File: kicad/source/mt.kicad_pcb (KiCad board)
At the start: 2 copper layers, 65 parts, among them IC1 MCP73831T-2ACI_OT, IC2 BQ29728DSER, IC3 TLV74333PDBVR, IC4 TLV9152IDR, IC5 MSPM0G3507SPMR, IC5 RT9167A-33GB, IC6 IS62WV1288BLL-55QLI, IC7 DAC082S085CIMMX_NOPB, IC8 SN74HC148NSR, IC8 TPS613222ADBVR, J1 694106301002, J2 SJ1-3524N, J3 Conn_01x05_MountingPin, J4 Conn_01x09_MountingPin, Q1 CSD16406Q3, Q2 CSD16406Q3, U1 1043

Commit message: completed full schematic
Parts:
- removed the C1 at (205.4, 44.4)
- removed the C1 at (205.4, 46.4)
- removed the C4 at (205.4, 50.3)
- removed the C4 at (111.7, 113.8)
- removed the C5 at (192.6, 59.5)
- removed the C5 at (121.5, 111.5)
- removed C6: 47u, Capacitor_SMD:C_0805_2012Metric
- removed C7: 4.7u, Capacitor_SMD:C_0402_1005Metric
- removed C7: 100n, Capacitor_SMD:C_1206_3216Metric
- removed C8: 10u, Capacitor_SMD:C_0603_1608Metric
- removed the IC5 at (149.8, 100.2)
- removed the IC5 at (183.8, 84.9)
- removed the IC8 at (183.8, 89.5)
- removed the IC8 at (177.9, 76.6)
- removed L1: 2.2u, Inductor_SMD:L_1008_2520Metric
- removed the R11 at (108.2, 110.3)
- removed the R11 at (108.2, 108.3)
- removed the R12 at (108.2, 106.3)
- removed the R12 at (108.2, 112.3)
- removed the R7 at (163.3, 96.7)
- removed the R7 at (108.2, 102.4)
- removed the R8 at (108.2, 104.4)
- removed the R8 at (163.3, 98.7)
- added C1: 10u, Capacitor_SMD:C_0402_1005Metric, F.Cu at (177.6, 58.8)
- added C21: 10u, Capacitor_SMD:C_0402_1005Metric, F.Cu at (183.3, 64.7)
- added C22: 10u, Capacitor_SMD:C_0402_1005Metric, F.Cu at (186.2, 58.8)
- added C23: 10u, Capacitor_SMD:C_0402_1005Metric, F.Cu at (186.2, 60.7)
- added C24: 10u, Capacitor_SMD:C_0402_1005Metric, F.Cu at (186.2, 62.7)
- added C25: 10u, Capacitor_SMD:C_0402_1005Metric, F.Cu at (186.2, 64.7)
- added C4: 10u, Capacitor_SMD:C_0402_1005Metric, F.Cu at (177.6, 62.7)
- added C5: 22u, Capacitor_SMD:C_0603_1608Metric, F.Cu at (191.3, 96.1)
- added IC10: SN74HC148NSR, SN74HC148NSR:SOIC127P780X200-16N, F.Cu at (122.2, 139.3)
- added IC11: SN74HC148NSR, SN74HC148NSR:SOIC127P780X200-16N, F.Cu at (132.7, 139.3)
- added IC5: MSPM0G3507SPMR, MSPM0G3507SPMR:QFP50P1200X1200X160-64N, F.Cu at (183.4, 50.5)
- added IC8: SN74HC148NSR, SN74HC148NSR:SOIC127P780X200-16N, F.Cu at (101.2, 139.3)
- added IC9: SN74HC148NSR, SN74HC148NSR:SOIC127P780X200-16N, F.Cu at (111.7, 139.3)
- added R11: 100k, Resistor_SMD:R_0402_1005Metric, F.Cu at (182.5, 106.0)
- added R12: 100k, Resistor_SMD:R_0402_1005Metric, F.Cu at (182.5, 108.0)
- added R15: 100k, Resistor_SMD:R_0402_1005Metric, F.Cu at (182.5, 114.0)
- added R16: 100k, Resistor_SMD:R_0402_1005Metric, F.Cu at (182.5, 115.9)
- added R17: 100k, Resistor_SMD:R_0402_1005Metric, F.Cu at (182.5, 117.9)
- added R18: 100k, Resistor_SMD:R_0402_1005Metric, F.Cu at (182.5, 119.9)
- added R19: 100k, Resistor_SMD:R_0402_1005Metric, F.Cu at (182.5, 121.9)
- added R20: 100k, Resistor_SMD:R_0402_1005Metric, F.Cu at (182.5, 123.9)
- added R21: 100k, Resistor_SMD:R_0402_1005Metric, F.Cu at (185.4, 106.0)
- added R22: 100k, Resistor_SMD:R_0402_1005Metric, F.Cu at (185.4, 108.0)
- added R23: 100k, Resistor_SMD:R_0402_1005Metric, F.Cu at (185.4, 110.0)
- added R24: 100k, Resistor_SMD:R_0402_1005Metric, F.Cu at (185.4, 112.0)
- added R25: 100k, Resistor_SMD:R_0402_1005Metric, F.Cu at (185.4, 114.0)
- added R26: 100k, Resistor_SMD:R_0402_1005Metric, F.Cu at (185.4, 115.9)
- added R27: 100k, Resistor_SMD:R_0402_1005Metric, F.Cu at (185.4, 117.9)
- added R28: 100k, Resistor_SMD:R_0402_1005Metric, F.Cu at (185.4, 119.9)
- added R29: 100k, Resistor_SMD:R_0402_1005Metric, F.Cu at (185.4, 121.9)
- added R30: 100k, Resistor_SMD:R_0402_1005Metric, F.Cu at (185.4, 123.9)
- added R31: 100k, Resistor_SMD:R_0402_1005Metric, F.Cu at (188.3, 106.0)
- added R32: 100k, Resistor_SMD:R_0402_1005Metric, F.Cu at (188.3, 108.0)
- added R33: 100k, Resistor_SMD:R_0402_1005Metric, F.Cu at (188.3, 110.0)
- added R34: 100k, Resistor_SMD:R_0402_1005Metric, F.Cu at (188.3, 112.0)
- added R35: 100k, Resistor_SMD:R_0402_1005Metric, F.Cu at (188.3, 114.0)
- added R36: 100k, Resistor_SMD:R_0402_1005Metric, F.Cu at (188.3, 115.9)
- added R37: 100k, Resistor_SMD:R_0402_1005Metric, F.Cu at (188.3, 117.9)
- added R38: 100k, Resistor_SMD:R_0402_1005Metric, F.Cu at (188.3, 119.9)
- added R39: 100k, Resistor_SMD:R_0402_1005Metric, F.Cu at (188.3, 121.9)
- added R40: 100k, Resistor_SMD:R_0402_1005Metric, F.Cu at (188.3, 123.9)
- added R41: 100k, Resistor_SMD:R_0402_1005Metric, F.Cu at (191.2, 106.0)
- added R42: 100k, Resistor_SMD:R_0402_1005Metric, F.Cu at (191.2, 108.0)
- added R43: 100k, Resistor_SMD:R_0402_1005Metric, F.Cu at (191.2, 110.0)
- added R44: 100k, Resistor_SMD:R_0402_1005Metric, F.Cu at (191.2, 112.0)
- added R45: 100k, Resistor_SMD:R_0402_1005Metric, F.Cu at (191.2, 114.0)
- added R46: 100k, Resistor_SMD:R_0402_1005Metric, F.Cu at (191.2, 115.9)
- added R47: 100k, Resistor_SMD:R_0402_1005Metric, F.Cu at (191.2, 117.9)
- added R48: 100k, Resistor_SMD:R_0402_1005Metric, F.Cu at (191.2, 119.9)
- added R49: 100k, Resistor_SMD:R_0402_1005Metric, F.Cu at (191.2, 121.9)
- added R7: 10k, Resistor_SMD:R_0402_1005Metric, F.Cu at (179.6, 117.9)
- added R8: 10k, Resistor_SMD:R_0402_1005Metric, F.Cu at (179.6, 119.9)
- added S10: TL6800AF160QJ, TL6800AF160QJ:TL6800AF160QJ, F.Cu at (114.9, 81.5)
- added S11: TL6800AF160QJ, TL6800AF160QJ:TL6800AF160QJ, F.Cu at (114.9, 91.0)
- added S12: TL6800AF160QJ, TL6800AF160QJ:TL6800AF160QJ, F.Cu at (114.9, 100.3)
- added S13: TL6800AF160QJ, TL6800AF160QJ:TL6800AF160QJ, F.Cu at (114.9, 109.8)
- added S14: TL6800AF160QJ, TL6800AF160QJ:TL6800AF160QJ, F.Cu at (114.9, 119.2)
- added S15: TL6800AF160QJ, TL6800AF160QJ:TL6800AF160QJ, F.Cu at (114.9, 128.6)
- added S16: TL6800AF160QJ, TL6800AF160QJ:TL6800AF160QJ, F.Cu at (127.5, 72.2)
- added S17: TL6800AF160QJ, TL6800AF160QJ:TL6800AF160QJ, F.Cu at (127.5, 81.5)
- added S18: TL6800AF160QJ, TL6800AF160QJ:TL6800AF160QJ, F.Cu at (127.5, 91.0)
- added S19: TL6800AF160QJ, TL6800AF160QJ:TL6800AF160QJ, F.Cu at (127.5, 100.3)
- added S20: TL6800AF160QJ, TL6800AF160QJ:TL6800AF160QJ, F.Cu at (127.5, 109.8)
- added S21: TL6800AF160QJ, TL6800AF160QJ:TL6800AF160QJ, F.Cu at (127.5, 119.2)
- added S22: TL6800AF160QJ, TL6800AF160QJ:TL6800AF160QJ, F.Cu at (127.5, 128.6)
- added S23: TL6800AF160QJ, TL6800AF160QJ:TL6800AF160QJ, F.Cu at (140.1, 72.2)
- added S24: TL6800AF160QJ, TL6800AF160QJ:TL6800AF160QJ, F.Cu at (140.1, 81.5)
- added S25: TL6800AF160QJ, TL6800AF160QJ:TL6800AF160QJ, F.Cu at (140.1, 91.0)
- added S26: TL6800AF160QJ, TL6800AF160QJ:TL6800AF160QJ, F.Cu at (140.1, 100.3)
- added S27: TL6800AF160QJ, TL6800AF160QJ:TL6800AF160QJ, F.Cu at (140.1, 109.8)
- added S28: TL6800AF160QJ, TL6800AF160QJ:TL6800AF160QJ, F.Cu at (140.1, 119.2)
- added S29: TL6800AF160QJ, TL6800AF160QJ:TL6800AF160QJ, F.Cu at (140.1, 128.6)
- added S3: TL6800AF160QJ, TL6800AF160QJ:TL6800AF160QJ, F.Cu at (102.3, 81.5)
- added S30: TL6800AF160QJ, TL6800AF160QJ:TL6800AF160QJ, F.Cu at (152.7, 72.2)
- added S31: TL6800AF160QJ, TL6800AF160QJ:TL6800AF160QJ, F.Cu at (152.7, 81.5)
- added S32: TL6800AF160QJ, TL6800AF160QJ:TL6800AF160QJ, F.Cu at (152.7, 91.0)
- added S33: TL6800AF160QJ, TL6800AF160QJ:TL6800AF160QJ, F.Cu at (152.7, 100.3)
- added S34: TL6800AF160QJ, TL6800AF160QJ:TL6800AF160QJ, F.Cu at (152.7, 109.8)
- added S35: TL6800AF160QJ, TL6800AF160QJ:TL6800AF160QJ, F.Cu at (152.7, 119.2)
- added S4: TL6800AF160QJ, TL6800AF160QJ:TL6800AF160QJ, F.Cu at (102.3, 91.0)
- added S5: TL6800AF160QJ, TL6800AF160QJ:TL6800AF160QJ, F.Cu at (102.3, 100.3)
- added S6: TL6800AF160QJ, TL6800AF160QJ:TL6800AF160QJ, F.Cu at (102.3, 109.8)
- added S7: TL6800AF160QJ, TL6800AF160QJ:TL6800AF160QJ, F.Cu at (102.3, 119.2)
- added S8: TL6800AF160QJ, TL6800AF160QJ:TL6800AF160QJ, F.Cu at (102.3, 128.6)
- added S9: TL6800AF160QJ, TL6800AF160QJ:TL6800AF160QJ, F.Cu at (114.9, 72.2)
- C20: value 22u -> 10u; footprint Capacitor_SMD:C_0603_1608Metric -> Capacitor_SMD:C_0402_1005Metric
- J3: value Conn_01x05_MountingPin -> Conn_01x05_Pin
- J4: value Conn_01x09_MountingPin -> Conn_01x09_Pin; footprint Connector_PinHeader_2.54mm:PinHeader_1x09_P2.54mm_Vertical -> Connector_PinSocket_2.54mm:PinSocket_1x09_P2.54mm_Vertical
- R5, R6: value 10k -> 100k
- moved C3 100.5 mm to (154.3, 134.9)
- moved C11 90.0 mm to (180.4, 60.7)
- moved C10 89.3 mm to (180.4, 58.8)
- moved C2 83.0 mm to (177.6, 60.7)
- moved C9 81.9 mm to (177.6, 64.7)
- moved R5 73.0 mm to (179.6, 114.0)
- moved R6 73.0 mm to (179.6, 115.9)
- moved R1 67.9 mm to (179.6, 106.0)
- moved R2 67.9 mm to (179.6, 108.0)
- moved R4 67.9 mm to (179.6, 112.0)
- moved R3 67.9 mm to (179.6, 110.0)
- moved J1 66.0 mm to (159.7, 135.8)
- moved J2 66.0 mm to (185.0, 134.0)
- moved S2 65.1 mm to (102.3, 72.2)
- moved S1 62.9 mm to (142.7, 137.1), turned to 0 degrees
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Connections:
- C15 pad 1: Net-(IC5-VDD) -> VDD
- C16 pad 1: Net-(IC5-VDD) -> VDD
- C18 pad 1: Net-(IC6-VDD) -> VDD
- C19 pad 1: Net-(IC6-VDD) -> VDD
- IC3 pad 1: VBAT -> Net-(IC3-EN)
- IC3 pad 3: VBAT -> Net-(IC3-EN)
- IC6 pad 13: unconnected-(IC6-I/O0-Pad13) -> I/O0
- IC6 pad 14: unconnected-(IC6-I/O1-Pad14) -> I/O1
- IC6 pad 15: unconnected-(IC6-I/O2-Pad15) -> I/O2
- IC6 pad 17: unconnected-(IC6-I/O3-Pad17) -> I/O3
- IC6 pad 18: unconnected-(IC6-I/O4-Pad18) -> I/O4
- IC6 pad 19: unconnected-(IC6-I/O5-Pad19) -> I/O5
- IC6 pad 20: unconnected-(IC6-I/O6-Pad20) -> I/O6
- IC6 pad 21: unconnected-(IC6-I/O7-Pad21) -> I/O7
- IC6 pad 22: unconnected-(IC6-~{CS1}-Pad22) -> GND
- IC6 pad 24: unconnected-(IC6-~{OE}-Pad24) -> GND
- IC6 pad 29: unconnected-(IC6-~{WE}-Pad29) -> RAM_WR
- IC6 pad 30: unconnected-(IC6-CS2-Pad30) -> RAM_EN
- IC6 pad 32: Net-(IC6-VDD) -> VDD
- IC7 pad 1: unconnected-(IC7-VA-Pad1) -> VDD
- IC7 pad 10: unconnected-(IC7-SCLK-Pad10) -> SPI1_SCK
- IC7 pad 6: unconnected-(IC7-GND-Pad6) -> GND
- IC7 pad 7: unconnected-(IC7-VREFIN-Pad7) -> VDD
- IC7 pad 8: unconnected-(IC7-DIN-Pad8) -> SPI1_PICO
- IC7 pad 9: unconnected-(IC7-~{SYNC}-Pad9) -> ~SYNC
- J4 pad 1: unconnected-(J4-Pin_1-Pad1) -> VDD
- J4 pad 3: unconnected-(J4-Pin_3-Pad3) -> GND
- J4 pad 4: unconnected-(J4-Pin_4-Pad4) -> SPI0_SCK
- J4 pad 5: unconnected-(J4-Pin_5-Pad5) -> SPI0_PICO
- J4 pad 6: unconnected-(J4-Pin_6-Pad6) -> SPI0_CS0
- R10 pad 2: GND -> VDD
- R13 pad 1: VDD -> Net-(J2-RING)
- R13 pad 2: NRST -> GND
- R14 pad 1: VDD -> Net-(J2-TIP)
- R14 pad 2: Net-(R14-Pad2) -> GND
- R5 pad 1: RV1A -> VBAT
- R5 pad 2: Net-(C9-Pad1) -> Net-(IC3-EN)
- R6 pad 1: Net-(C10-Pad1) -> VBAT
- R6 pad 2: RV2A -> GND
- R9 pad 1: Net-(IC4-IN1+) -> VDD
- R9 pad 2: GND -> Net-(IC4-IN1+)
- S1 pad 2: VBAT -> Net-(IC3-EN)
- S2 pad 1: Net-(R14-Pad2) -> Net-(IC8-0)
- S2 pad 2: Net-(R14-Pad2) -> Net-(IC8-0)

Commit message: configured PCB with 4-layer stackup and JLCPCB DRC rules
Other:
- copper layers 2 -> 4
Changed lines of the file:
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@@
 	(layers
 		(0 "F.Cu" signal)
+		(4 "In1.Cu" signal)
+		(6 "In2.Cu" signal)
 		(2 "B.Cu" signal)
 		(9 "F.Adhes" user "F.Adhesive")
@@
 	)
 	(setup
+		(stackup
+			(layer "F.SilkS"
+				(type "Top Silk Screen")
+			)
+			(layer "F.Paste"
+				(type "Top Solder Paste")
+			)
+			(layer "F.Mask"
+				(type "Top Solder Mask")
+				(thickness 0.01)
+			)
+			(layer "F.Cu"
+				(type "copper")
+				(thickness 0.035)
+			)
+			(layer "dielectric 1"
+				(type "prepreg")
+				(thickness 0.1)
+				(material "FR4")
+				(epsilon_r 4.5)
+				(loss_tangent 0.02)
+			)
+			(layer "In1.Cu"
+				(type "copper")
+				(thickness 0.035)
+			)
+			(layer "dielectric 2"
+				(type "core")
+				(thickness 1.24)
+				(material "FR4")
+				(epsilon_r 4.5)
+				(loss_tangent 0.02)
+			)
+			(layer "In2.Cu"
+				(type "copper")
+				(thickness 0.035)
+			)
+			(layer "dielectric 3"
+				(type "prepreg")
+				(thickness 0.1)
+				(material "FR4")
+				(epsilon_r 4.5)
+				(loss_tangent 0.02)
+			)
+			(layer "B.Cu"
+				(type "copper")
+				(thickness 0.035)
+			)
+			(layer "B.Mask"
+				(type "Bottom Solder Mask")
+				(thickness 0.01)
+			)
+			(layer "B.Paste"
+				(type "Bottom Solder Paste")
+			)
+			(layer "B.SilkS"
+				(type "Bottom Silk Screen")
+			)
+			(copper_finish "None")
+			(dielectric_constraints no)
+		)
 		(pad_to_mask_clearance 0)
 		(allow_soldermask_bridges_in_footprints no)

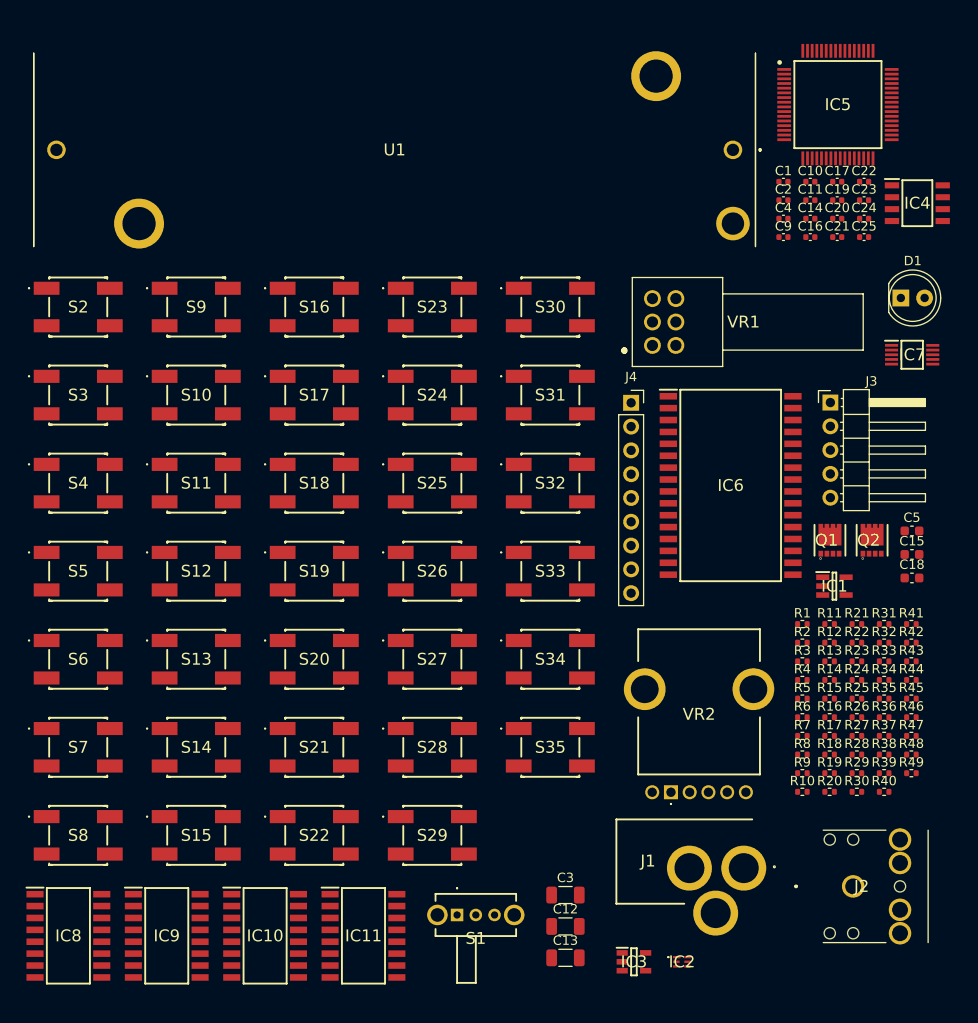
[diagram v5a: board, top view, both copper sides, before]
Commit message: added input OVP, screen config jumpers
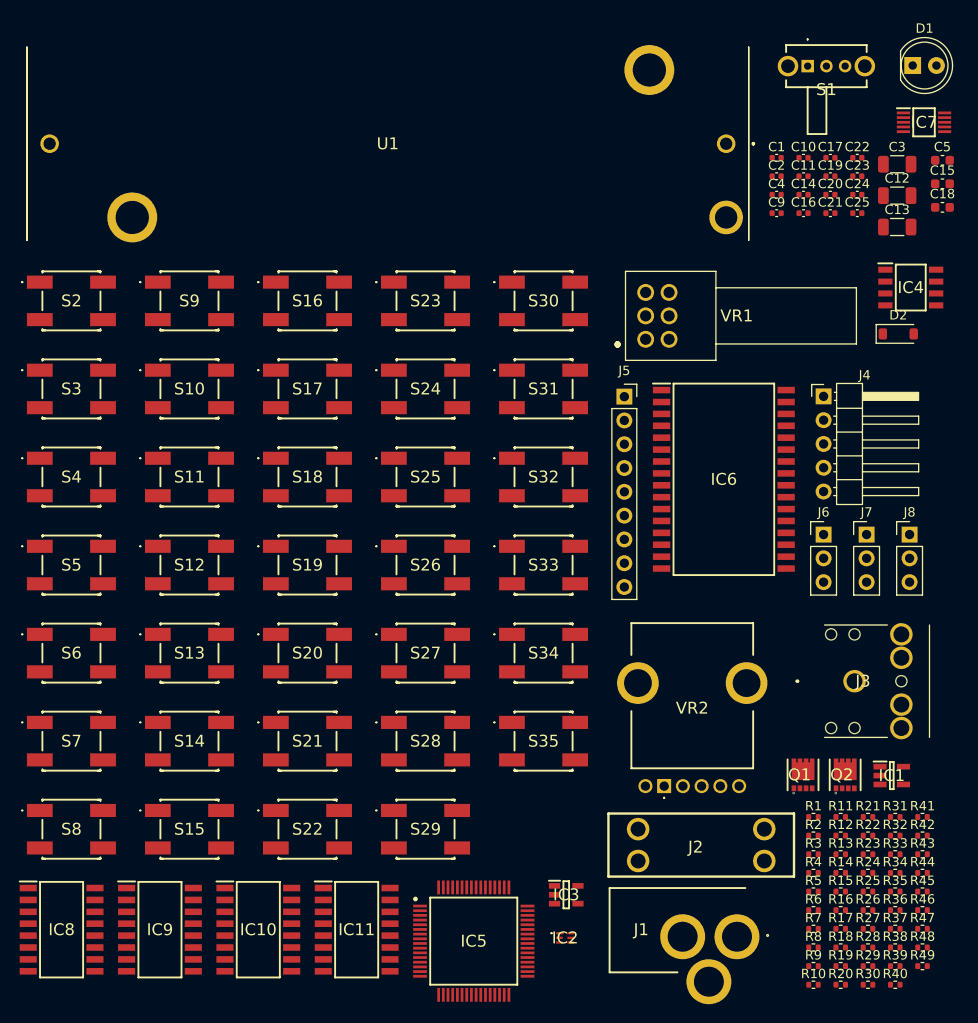
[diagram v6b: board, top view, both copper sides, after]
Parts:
- added D2: 5.6, Diode_SMD:D_SOD-123, F.Cu at (189.8, 75.0)
- added J5: Conn_01x09_Pin, Connector_PinSocket_2.54mm:PinSocket_1x09_P2.54mm_Vertical, F.Cu at (160.6, 81.7)
- added J6: Conn_01x03_Pin, Connector_PinHeader_2.54mm:PinHeader_1x03_P2.54mm_Vertical, F.Cu at (181.8, 96.4)
- added J7: Conn_01x03_Pin, Connector_PinHeader_2.54mm:PinHeader_1x03_P2.54mm_Vertical, F.Cu at (186.4, 96.4)
- added J8: Conn_01x03_Pin, Connector_PinHeader_2.54mm:PinHeader_1x03_P2.54mm_Vertical, F.Cu at (191.0, 96.4)
- J2: value SJ1-3524N -> 3557-2; footprint SJ1-3524N:SJ13524N -> 3557-2:3557-2
- J3: value Conn_01x05_Pin -> SJ1-3524N; footprint Connector_PinHeader_2.54mm:PinHeader_1x05_P2.54mm_Horizontal -> SJ1-3524N:SJ13524N
- J4: value Conn_01x09_Pin -> Conn_01x05_Pin; footprint Connector_PinSocket_2.54mm:PinSocket_1x09_P2.54mm_Vertical -> Connector_PinHeader_2.54mm:PinHeader_1x05_P2.54mm_Horizontal
- moved S1 98.0 mm to (180.1, 46.4)
- moved IC5 97.4 mm to (144.5, 139.8)
- moved C12 85.7 mm to (189.7, 60.3)
- moved C3 85.7 mm to (189.7, 56.9)
- moved C13 85.7 mm to (189.7, 63.6)
- moved C18 39.7 mm to (194.5, 61.5)
- moved C5 39.7 mm to (194.5, 56.5)
- moved C15 39.7 mm to (194.5, 59.0)
- moved J3 29.9 mm to (185.1, 112.1)
- moved Q1 25.2 mm to (179.6, 122.1)
- moved Q2 25.2 mm to (184.1, 122.1)
- moved IC7 24.8 mm to (192.6, 52.4)
- moved D1 24.8 mm to (191.3, 46.4)
- moved IC1 21.1 mm to (189.1, 122.2)
- moved R12 20.6 mm to (183.7, 128.6)
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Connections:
- C12 pad 2: Net-(J2-TIP) -> Net-(J3-TIP)
- C13 pad 2: Net-(J2-RING) -> Net-(J3-RING)
- J1 pad 1: Net-(D1-A) -> Net-(J1-POWER)
- J2 pad 1: GND -> Net-(J1-POWER)
- J2 pad 2: Net-(J2-TIP) -> Net-(D1-A)
- J2 pad 3: Net-(J2-RING) -> Net-(J1-POWER)
- J2 pad 4: unconnected-(J2-TIP_SWITCH-Pad4) -> Net-(D1-A)
- J3 pad 2: VDD -> Net-(J3-TIP)
- J3 pad 3: NRST -> Net-(J3-RING)
- J3 pad 4: SWDIO -> unconnected-(J3-TIP_SWITCH-Pad4)
- J3 pad 5: SWCLK -> unconnected-(J3-NP-Pad5)
- J4 pad 1: VDD -> GND
- J4 pad 2: unconnected-(J4-Pin_2-Pad2) -> VDD
- J4 pad 3: GND -> NRST
- J4 pad 4: SPI0_SCK -> SWDIO
- J4 pad 5: SPI0_PICO -> SWCLK
- R13 pad 1: Net-(J2-RING) -> Net-(J3-RING)
- R14 pad 1: Net-(J2-TIP) -> Net-(J3-TIP)

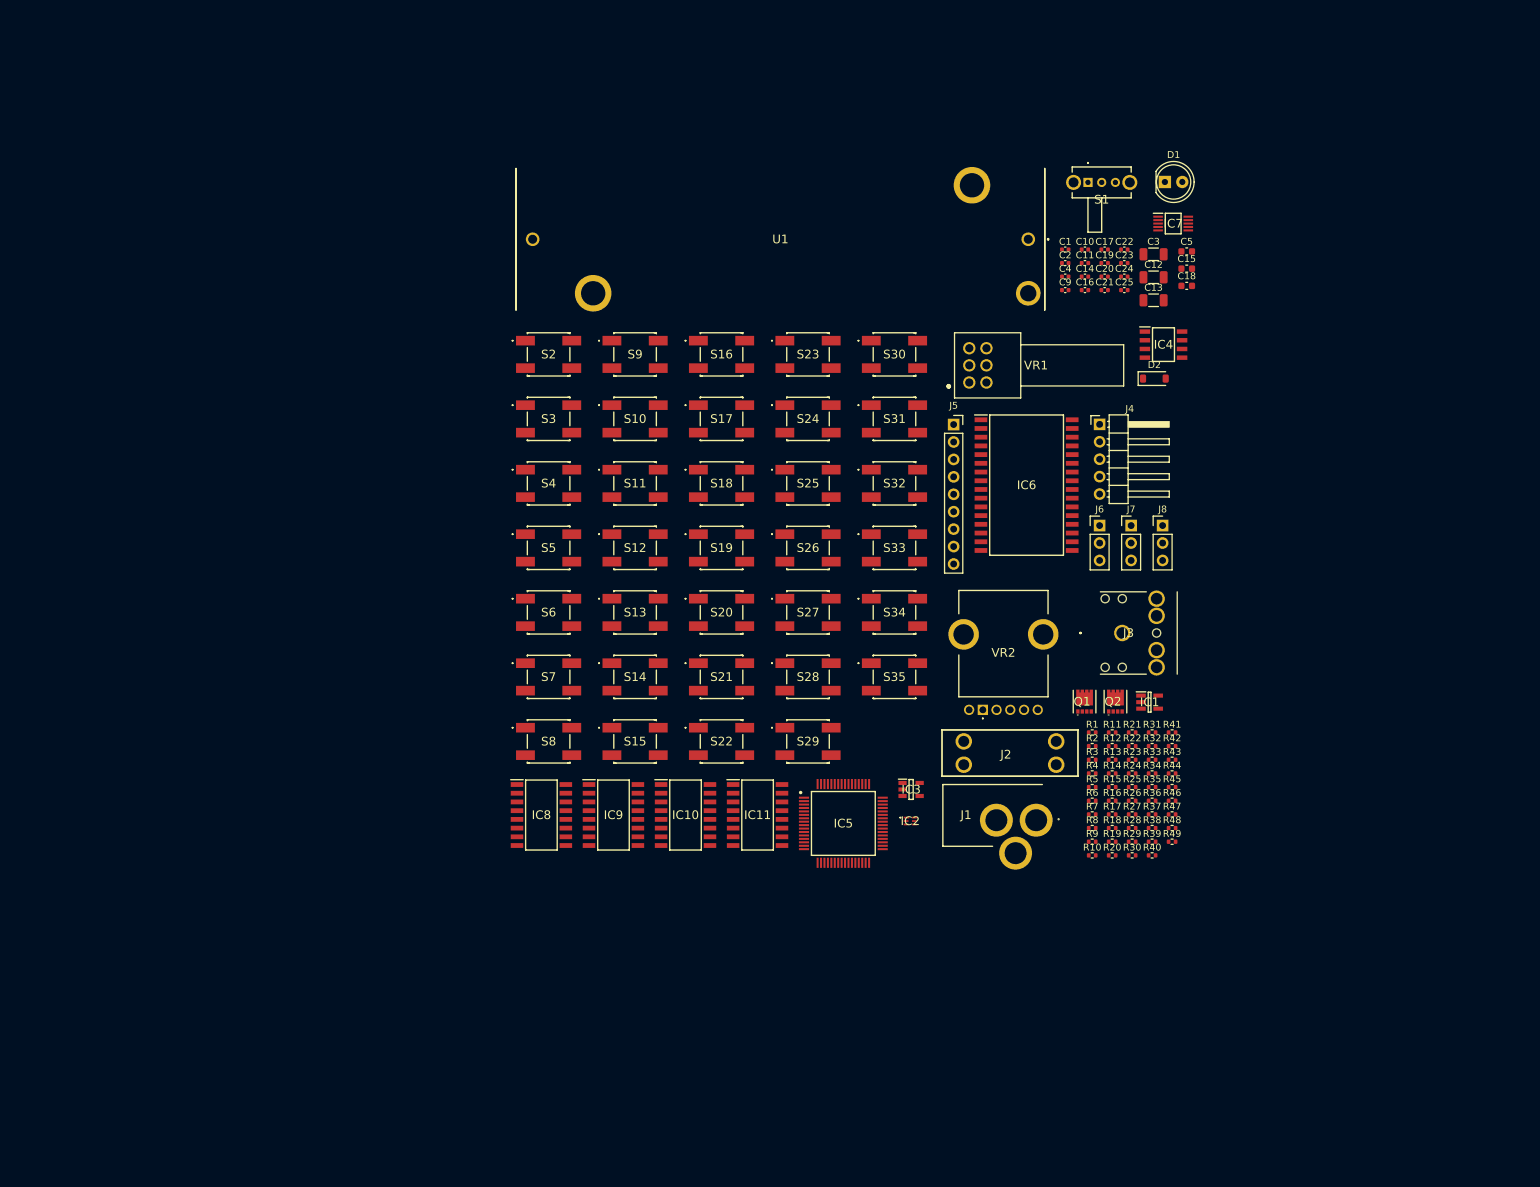
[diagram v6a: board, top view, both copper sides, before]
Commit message: started routing SRAM on PCB
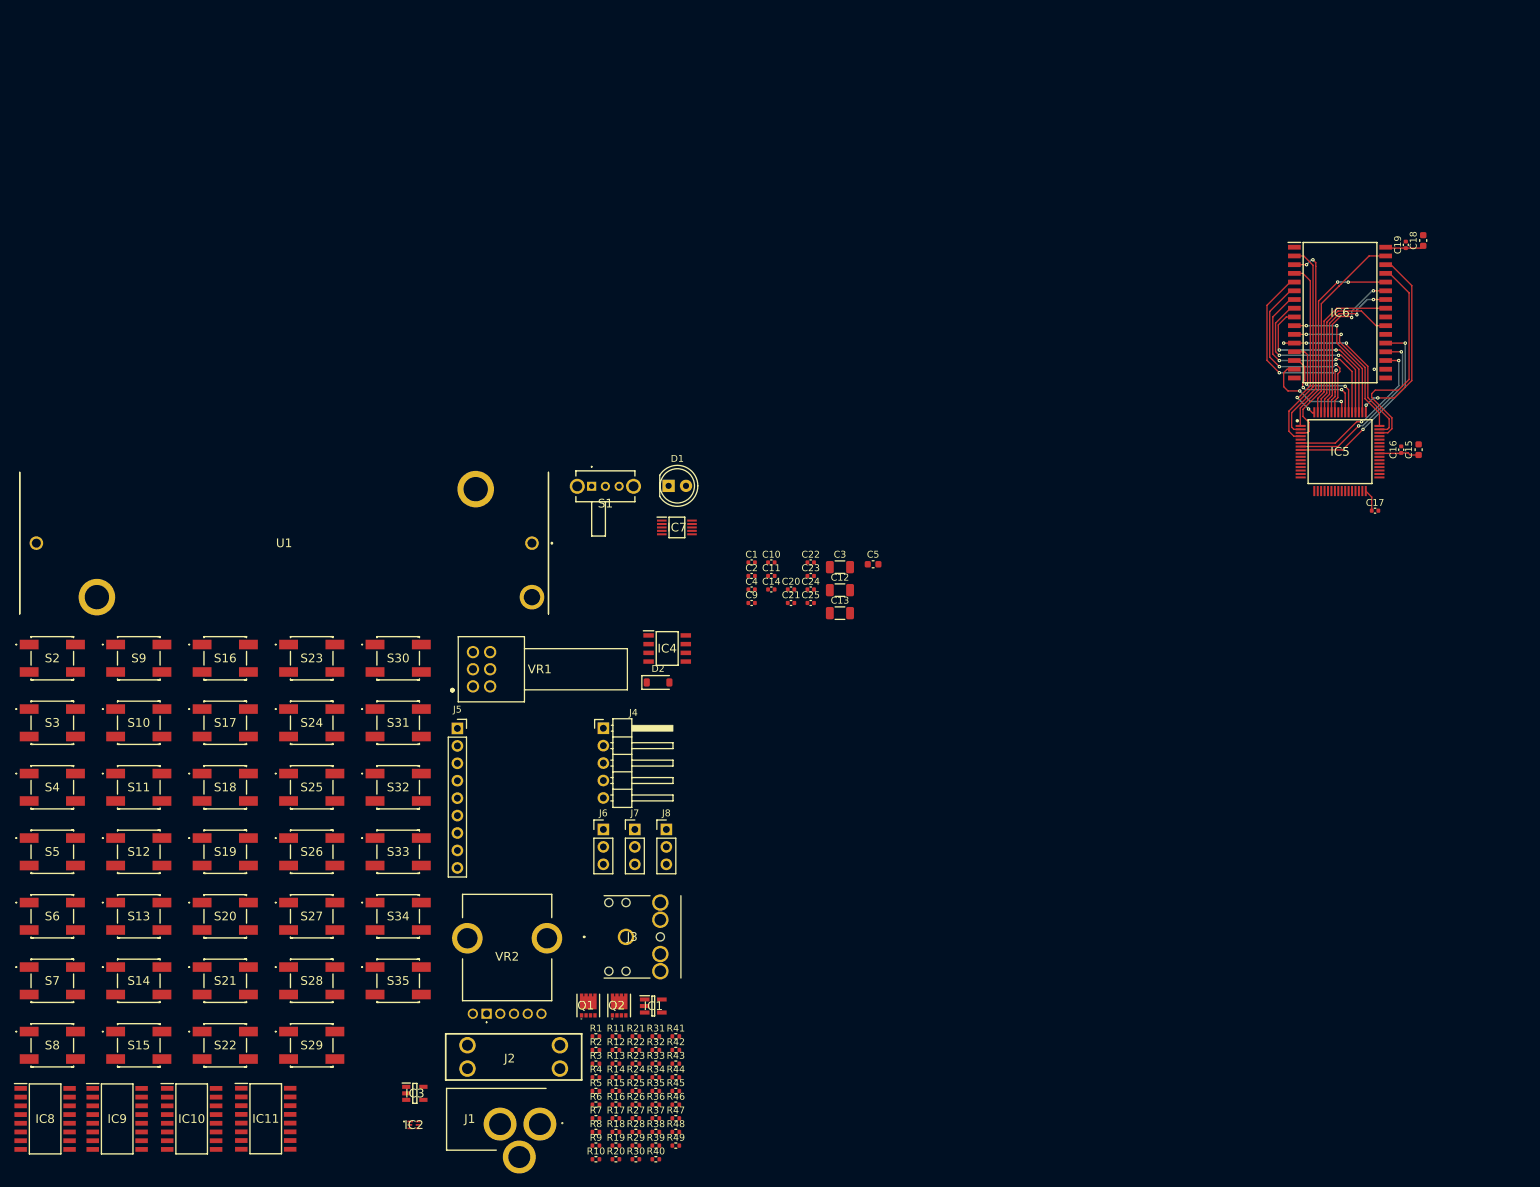
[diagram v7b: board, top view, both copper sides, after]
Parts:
- moved IC5 90.4 mm to (216.9, 85.7)
- moved IC4 84.8 mm to (118.8, 114.4)
- moved IC7 84.8 mm to (120.2, 96.7)
- moved J3 84.8 mm to (112.8, 156.4)
- moved J6 84.8 mm to (109.5, 140.7)
- moved J7 84.8 mm to (114.1, 140.7)
- moved J8 84.8 mm to (118.7, 140.7)
- moved Q1 84.8 mm to (107.3, 166.4)
- moved Q2 84.8 mm to (111.8, 166.4)
- moved R21 84.8 mm to (114.3, 170.9)
- moved R23 84.8 mm to (114.3, 174.9)
- moved R24 84.8 mm to (114.3, 176.8)
- moved R26 84.8 mm to (114.3, 180.8)
- moved R27 84.8 mm to (114.3, 182.8)
- moved R29 84.8 mm to (114.3, 186.8)
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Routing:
- net A15: track 0.00 -> 33.6 mm
- net RAM_WR: track 0.00 -> 31.9 mm
- net A16: track 0.00 -> 31.5 mm
- net A7: track 0.00 -> 30.8 mm, vias 0 -> 2
- net A14: track 0.00 -> 30.5 mm, vias 0 -> 2
- net A13: track 0.00 -> 30.3 mm, vias 0 -> 2
- net A6: track 0.00 -> 29.4 mm, vias 0 -> 2
- net I/O7: track 0.00 -> 28.3 mm, vias 0 -> 2
- net A5: track 0.00 -> 28.3 mm, vias 0 -> 2
- net RAM_EN: track 0.00 -> 28.1 mm, vias 0 -> 2
- net A4: track 0.00 -> 26.8 mm, vias 0 -> 2
- net I/O6: track 0.00 -> 25.8 mm, vias 0 -> 2
- net A3: track 0.00 -> 25.6 mm, vias 0 -> 2
- net A0: track 0.00 -> 25.6 mm, vias 0 -> 3
- net A12: track 0.00 -> 24.1 mm, vias 0 -> 2
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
